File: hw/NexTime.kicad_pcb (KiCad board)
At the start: 4 copper layers, 84.2 x 43.2 mm, 74 parts, among them J101 CR2032, J102 pwr+data, U101 SRV05-4, U102 XTAA5212IRGER, U103 ESP32-S3-WROOM-1-N8R8, U104 OPA4863, U105 LMR51430YDDCR, U106 TPS74633PQWDRBRQ1, Y101 RV-3032-C7_32.768kHz-2.5PPM-T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

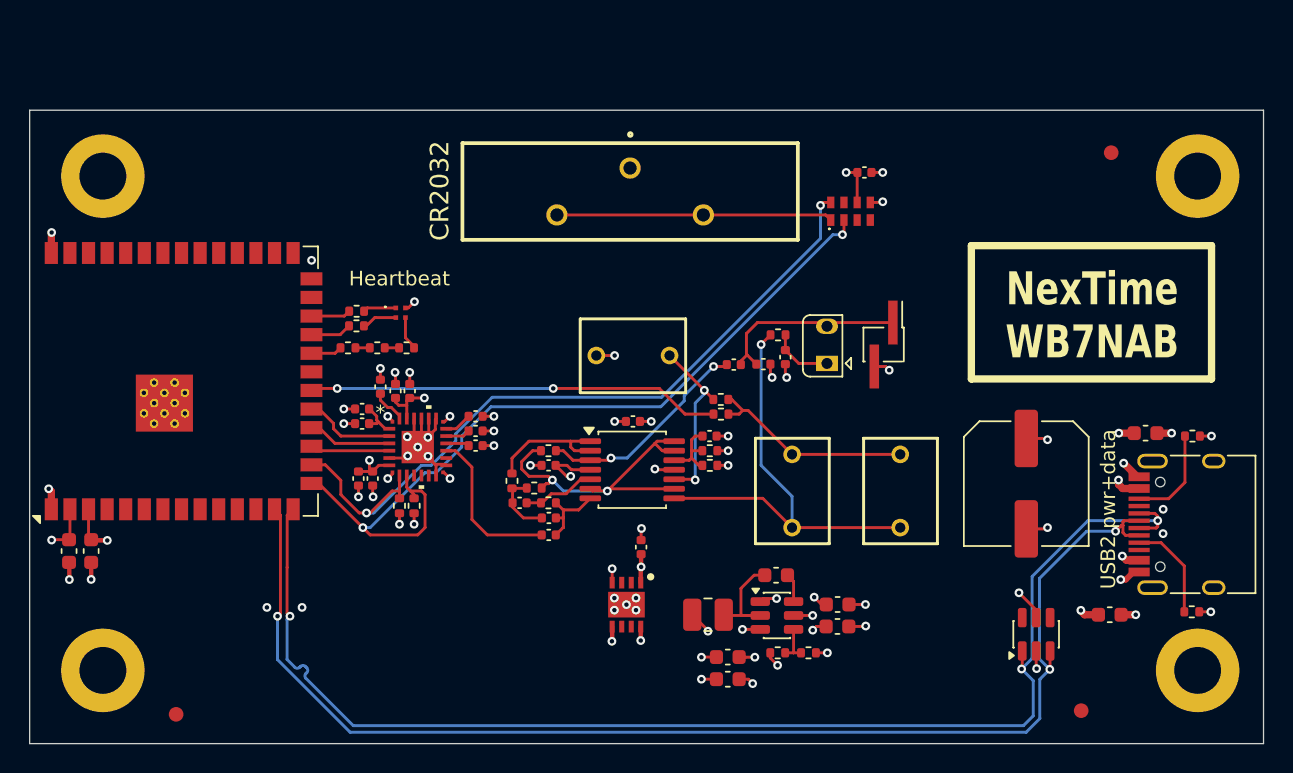
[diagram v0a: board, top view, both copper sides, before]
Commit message: Added RECOVER pushbutton. Cleared the way for display but not added yet.
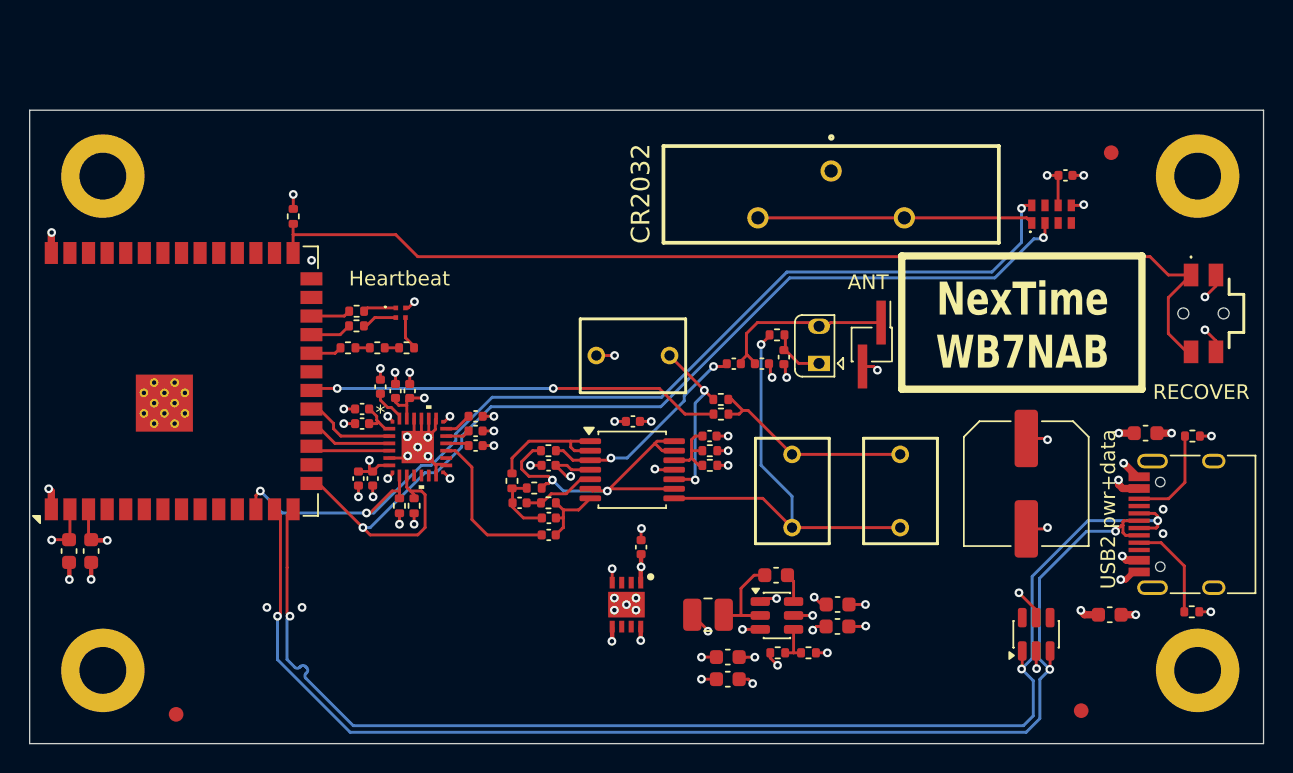
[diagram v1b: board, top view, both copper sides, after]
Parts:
- added R227: 10k, Resistor_SMD:R_0402_1005Metric, F.Cu at (67.6, 97.4)
- added SW201: Push button switch, Library:EVQPUC02K, F.Cu at (129.8, 104.0)
- moved C105 13.7 mm to (120.3, 94.6)
- moved J101 13.7 mm to (104.3, 95.9)
- moved Y101 13.7 mm to (119.4, 97.2)
- moved L101 0.81 mm to (107.1, 106.2)
- moved D102 0.54 mm to (103.5, 107.4)
- moved C121 0.10 mm to (99.6, 107.5)
- moved C125 0.10 mm to (101.1, 107.0)
- moved R114 0.07 mm to (100.6, 105.5)
- moved C117 0.06 mm to (97.7, 107.5)
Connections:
- U103 pad 12: unconnected-(U103-IO8-Pad12) -> /SCL
- U103 pad 16: /SCL -> unconnected-(U103-IO46-Pad16)
- U103 pad 27: unconnected-(U103-IO0-Pad27) -> /BOOT0
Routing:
- net /BOOT0: track 0.00 -> 71.2 mm
- net /SCL: track 52.2 -> 69.2 mm, vias 2 -> 3
- net /SDA: track 56.6 -> 70.2 mm
- net GND: track 53.9 -> 57.5 mm, vias 60 -> 62
- net +3.3V: track 21.9 -> 22.9 mm, vias 12 -> 13

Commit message: Update 3d models for parts. Display conn still missing
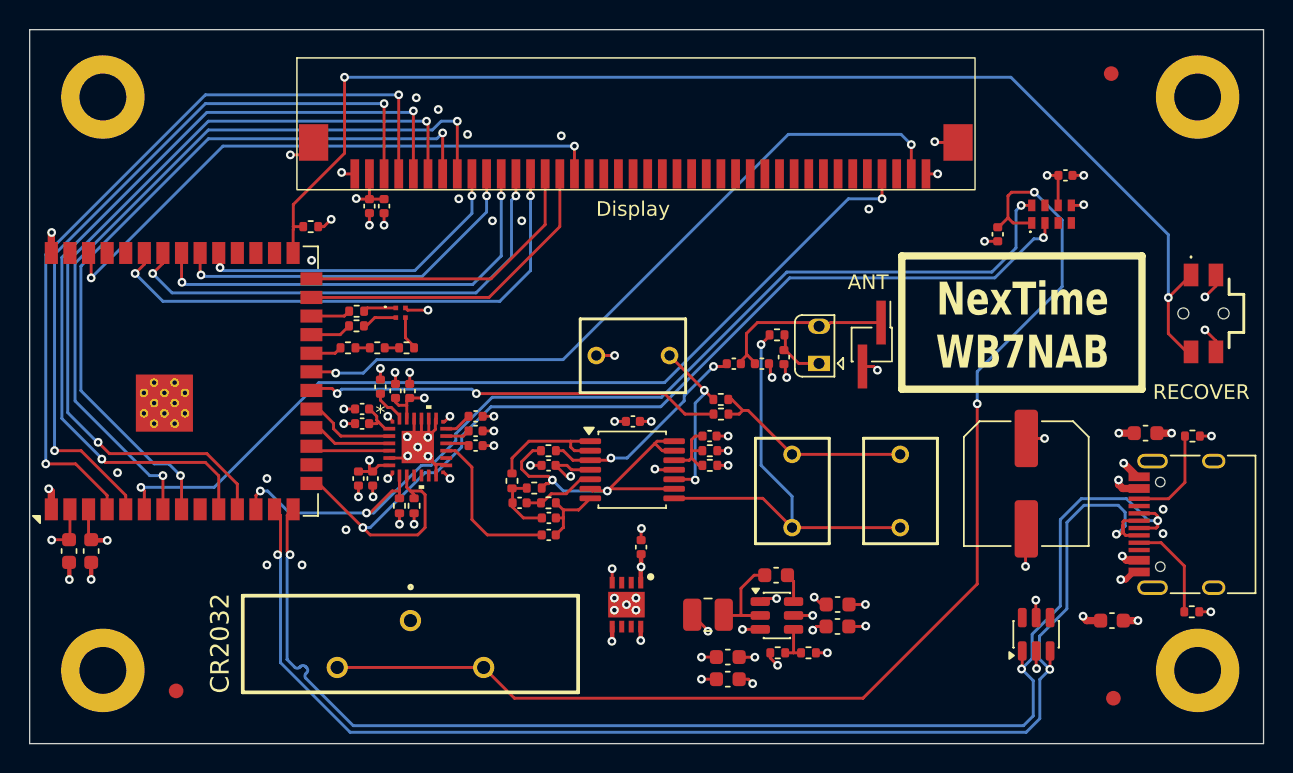
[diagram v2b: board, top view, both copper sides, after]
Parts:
- added C106: 10uF, Capacitor_SMD:C_0402_1005Metric, F.Cu at (73.8, 96.7)
- added C107: 100nF, Capacitor_SMD:C_0402_1005Metric, F.Cu at (72.8, 96.7)
- added C115: 100nF, Capacitor_SMD:C_0402_1005Metric, F.Cu at (115.7, 98.6)
- added J101: ER-CON40HB-2, Library:ER-CON40HB-2, F.Cu at (71.5, 95.5)
- moved J103 42.0 mm to (75.6, 126.6)
- moved H102 5.40 mm to (129.3, 89.2)
- moved H103 5.40 mm to (54.6, 89.2)
- moved FID102 5.40 mm to (123.5, 87.7)
- moved FID101 2.36 mm to (123.6, 130.3)
- moved FID103 1.60 mm to (59.6, 129.8)
- moved R107 1.38 mm to (68.8, 98.1), turned to 180 degrees
- moved C102 0.43 mm to (123.5, 125.0)
- renumbered C106 to C105, C107 to C108, C108 to C109, C109 to C110, C110 to C111, C111 to C112, C112 to C113, C113 to C114, C105 to C116, C116 to C117, C114 to C118, C115 to C119, C117 to C120, C118 to C121, C119 to C122, C120 to C123, C121 to C124, C122 to C125, C123 to C126, C124 to C127, C125 to C128, C126 to C129, C127 to C130, C128 to C131, C129 to C132, C130 to C133, C131 to C134, C132 to C135, C133 to C136, C134 to C137, D102 to D101, D101 to D102, J101 to J103, R115 to R103, R116 to R104, R108 to R105, R109 to R106, R227 to R107, R110 to R108, R111 to R109, R112 to R110, R113 to R111, R114 to R112, R103 to R113, R104 to R114, R105 to R115, R106 to R116, R107 to R118, R118 to R119, R119 to R120, R120 to R121, SW201 to SW101
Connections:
- net /bluLED renamed /bluHB
- net /grnLED renamed /grnHB
- net /redLED renamed /redHB
- U103 pad 10: unconnected-(U103-IO17-Pad10) -> /dispNRD
- U103 pad 11: unconnected-(U103-IO18-Pad11) -> /dispNWR
- U103 pad 21: unconnected-(U103-IO13-Pad21) -> /blPWM
- U103 pad 25: unconnected-(U103-IO48-Pad25) -> /dispD6
- U103 pad 26: unconnected-(U103-IO45-Pad26) -> /dispD5
- U103 pad 31: unconnected-(U103-IO38-Pad31) -> /dispD0
- U103 pad 32: unconnected-(U103-IO39-Pad32) -> /dispD1
- U103 pad 33: unconnected-(U103-IO40-Pad33) -> /dispD2
- U103 pad 34: unconnected-(U103-IO41-Pad34) -> /dispD3
- U103 pad 35: unconnected-(U103-IO42-Pad35) -> /dispD4
- U103 pad 38: unconnected-(U103-IO2-Pad38) -> /dispD7
- U103 pad 4: unconnected-(U103-IO4-Pad4) -> /dispDC
- U103 pad 5: unconnected-(U103-IO5-Pad5) -> /dispNCS
- U103 pad 6: unconnected-(U103-IO6-Pad6) -> /dispBUSY
- U103 pad 7: unconnected-(U103-IO7-Pad7) -> /dispTE
- U103 pad 8: unconnected-(U103-IO15-Pad8) -> /dispNRST
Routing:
- net Net-(Y101-VBACKUP): track 18.8 -> 83.8 mm, vias 0 -> 2
- net /dispBUSY: track 0.00 -> 62.1 mm, vias 0 -> 2
- net /dispNRD: track 0.00 -> 58.1 mm, vias 0 -> 2
- net /dispNWR: track 0.00 -> 57.7 mm, vias 0 -> 2
- net /dispDC: track 0.00 -> 54.3 mm, vias 0 -> 2
- net /dispTE: track 0.00 -> 53.5 mm, vias 0 -> 2
- net /dispNCS: track 0.00 -> 52.0 mm, vias 0 -> 2
- net /dispNRST: track 0.00 -> 51.3 mm, vias 0 -> 2
- net /blPWM: track 0.00 -> 50.0 mm, vias 0 -> 2
- net /dispD7: track 0.00 -> 40.1 mm, vias 0 -> 2
- net /dispD4: track 0.00 -> 36.9 mm, vias 0 -> 2
- net /dispD3: track 0.00 -> 33.6 mm, vias 0 -> 2
- net /dispD2: track 0.00 -> 30.3 mm, vias 0 -> 2
- net /dispD1: track 0.00 -> 25.5 mm, vias 0 -> 2
- net /dispD0: track 0.00 -> 22.6 mm, vias 0 -> 2
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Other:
- board size 84.2 x 43.2 mm -> 84.2 x 48.8 mm
